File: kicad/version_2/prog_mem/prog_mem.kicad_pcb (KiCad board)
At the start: 2 copper layers, 157.5 x 127.5 mm, 37 parts

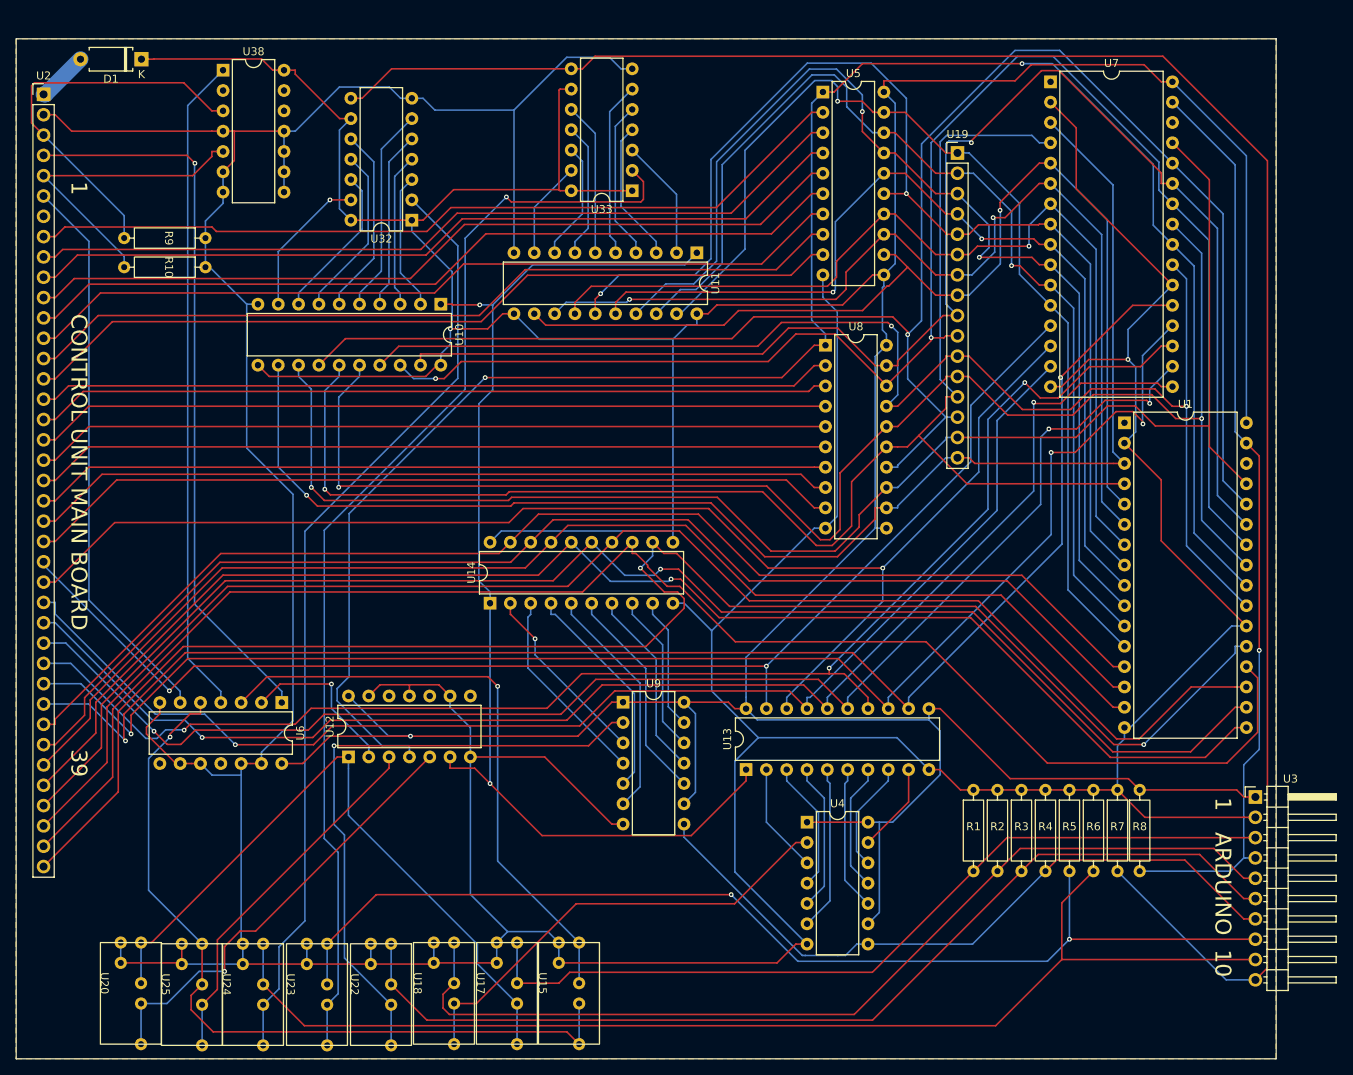
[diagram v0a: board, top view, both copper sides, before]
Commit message: Fixed prog mem and updated PCB
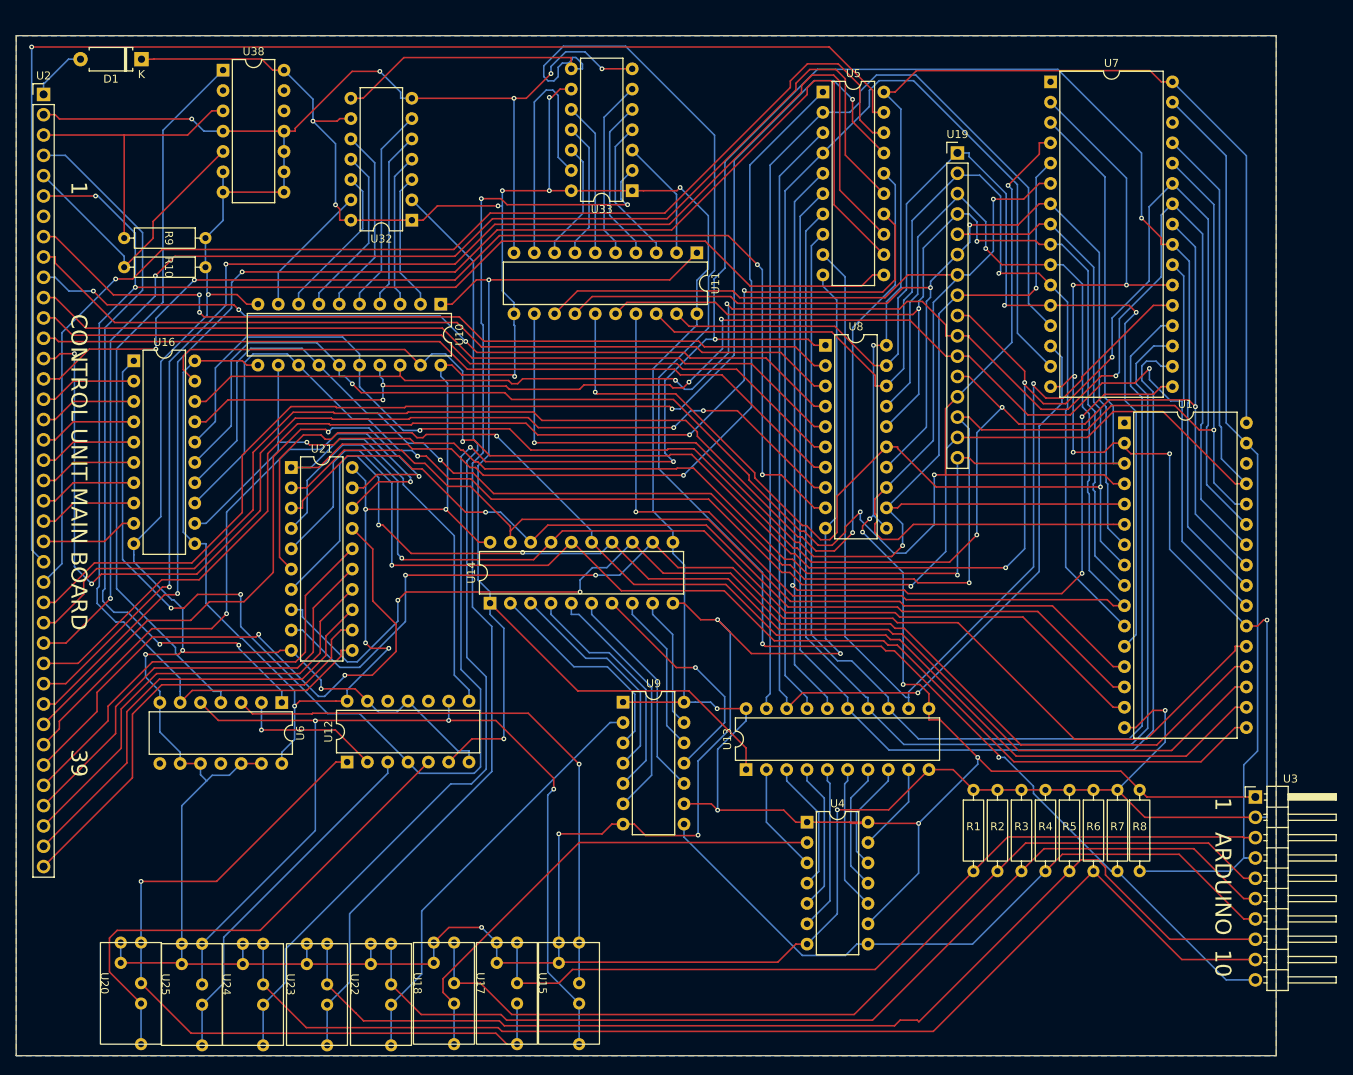
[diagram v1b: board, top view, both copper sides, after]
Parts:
- added U16: ~, Package_DIP:DIP-20_W7.62mm, F.Cu at (76.2, 71.8)
- added U21: ~, Package_DIP:DIP-20_W7.62mm, F.Cu at (95.9, 85.1)
- moved U12 0.66 mm to (102.9, 121.9)
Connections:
- U12 pad 8: unconnected-(U12-03-Pad8) -> Net-(U12-03)
- U12 pad 9: Net-(U1-A16) -> Net-(U12-I3)
- U15 pad 3: Net-(U15-OUT) -> Net-(U12-I3)
- U2 pad 16: Net-(U2-A8) -> Net-(U16-D0)
- U2 pad 17: Net-(U2-A9) -> Net-(U16-D1)
- U2 pad 18: Net-(U2-A10) -> Net-(U16-D2)
- U2 pad 19: Net-(U2-A11) -> Net-(U16-D3)
- U2 pad 20: Net-(U2-A12) -> Net-(U16-D4)
- U2 pad 21: Net-(U2-A13) -> Net-(U16-D5)
- U2 pad 22: Net-(U2-A14) -> Net-(U16-D6)
- U2 pad 23: Net-(U2-A15) -> Net-(U16-D7)
- U2 pad 24: Net-(U13-Q0) -> Net-(U2-D0)
- U2 pad 25: Net-(U13-Q1) -> Net-(U2-D1)
- U2 pad 26: Net-(U13-Q2) -> Net-(U2-D2)
- U2 pad 27: Net-(U13-Q3) -> Net-(U2-D3)
- U2 pad 28: Net-(U13-Q4) -> Net-(U2-D4)
- U2 pad 29: Net-(U13-Q5) -> Net-(U2-D5)
- U2 pad 30: Net-(U13-Q6) -> Net-(U2-D6)
- U2 pad 31: Net-(U13-Q7) -> Net-(U2-D7)
- U2 pad 32: Net-(U1-DQ0) -> Net-(U2-D8)
- U2 pad 33: Net-(U1-DQ1) -> Net-(U2-D9)
- U2 pad 34: Net-(U1-DQ2) -> Net-(U2-D10)
- U2 pad 35: Net-(U1-DQ3) -> Net-(U2-D11)
- U2 pad 36: Net-(U1-DQ4) -> Net-(U2-D12)
- U2 pad 37: Net-(U1-DQ5) -> Net-(U2-D13)
- U2 pad 38: Net-(U1-DQ6) -> Net-(U2-D14)
- U2 pad 39: Net-(U1-DQ7) -> Net-(U2-D15)
- U25 pad 1: Net-(U15-OUT) -> Net-(U12-I3)
- U5 pad 1: Net-(U1-OE#) -> Net-(U12-03)
- U5 pad 11: Net-(D1-K) -> Net-(U2-Done)
- U5 pad 12: Net-(U1-A7) -> Net-(U2-D7)
- U5 pad 13: Net-(U1-A6) -> Net-(U2-D6)
- U5 pad 14: Net-(U1-A5) -> Net-(U2-D5)
- U5 pad 15: Net-(U1-A4) -> Net-(U2-D4)
- U5 pad 16: Net-(U1-A3) -> Net-(U2-D3)
- U5 pad 17: Net-(U1-A2) -> Net-(U2-D2)
- U5 pad 18: Net-(U1-A1) -> Net-(U2-D1)
- U5 pad 19: Net-(U1-A0) -> Net-(U2-D0)
- U5 pad 2: Net-(U2-A0) -> Net-(U13-Q0)
- U5 pad 3: Net-(U2-A1) -> Net-(U13-Q1)
- U5 pad 4: Net-(U2-A2) -> Net-(U13-Q2)
- U5 pad 5: Net-(U2-A3) -> Net-(U13-Q3)
- U5 pad 6: Net-(U2-A4) -> Net-(U13-Q4)
- U5 pad 7: Net-(U2-A5) -> Net-(U13-Q5)
- U5 pad 8: Net-(U2-A6) -> Net-(U13-Q6)
- U5 pad 9: Net-(U2-A7) -> Net-(U13-Q7)
- U6 pad 5: Net-(U15-OUT) -> Net-(U12-I3)
- U8 pad 12: Net-(U1-A15) -> Net-(U1-A7)
- U8 pad 13: Net-(U1-A14) -> Net-(U1-A6)
- U8 pad 14: Net-(U1-A13) -> Net-(U1-A5)
- U8 pad 15: Net-(U1-A12) -> Net-(U1-A4)
- U8 pad 16: Net-(U1-A11) -> Net-(U1-A3)
- U8 pad 17: Net-(U1-A10) -> Net-(U1-A2)
- U8 pad 18: Net-(U1-A9) -> Net-(U1-A1)
- U8 pad 19: Net-(U1-A8) -> Net-(U1-A0)
- U8 pad 2: Net-(U2-A8) -> Net-(U2-A0)
- U8 pad 3: Net-(U2-A9) -> Net-(U2-A1)
- U8 pad 4: Net-(U2-A10) -> Net-(U2-A2)
- U8 pad 5: Net-(U2-A11) -> Net-(U2-A3)
- U8 pad 6: Net-(U2-A12) -> Net-(U2-A4)
- U8 pad 7: Net-(U2-A13) -> Net-(U2-A5)
- U8 pad 8: Net-(U2-A14) -> Net-(U2-A6)
- U8 pad 9: Net-(U2-A15) -> Net-(U2-A7)
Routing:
- net Net-(U2-D0): track 0.00 -> 176.5 mm, vias 0 -> 1
- net Net-(U2-D7): track 0.00 -> 174.5 mm, vias 0 -> 2
- net Net-(U2-D3): track 0.00 -> 173.5 mm, vias 0 -> 1
- net Net-(U2-D6): track 0.00 -> 172.7 mm, vias 0 -> 2
- net Net-(U2-D4): track 0.00 -> 167.6 mm, vias 0 -> 2
- net Net-(U2-D2): track 0.00 -> 156.2 mm, vias 0 -> 2
- net Net-(U12-03): track 0.00 -> 155.9 mm, vias 0 -> 1
- net Net-(U2-D1): track 0.00 -> 155.3 mm, vias 0 -> 1
- net Net-(U2-D5): track 0.00 -> 147.4 mm, vias 0 -> 2
- net Net-(U2-Done): track 70.4 -> 202.4 mm, vias 0 -> 2
- net Net-(U12-I3): track 0.00 -> 124.5 mm, vias 0 -> 3
- net Net-(U2-A15): track 102.4 -> 0.00 mm
- net Net-(U2-A14): track 100.8 -> 0.00 mm
- net Net-(U15-OUT): track 100.5 -> 0.00 mm, vias 1 -> 0
- net Net-(U2-A9): track 99.5 -> 0.00 mm
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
